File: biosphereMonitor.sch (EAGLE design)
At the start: 62 parts, among them IC1 XMEGA32A4AU, IC2 LM35, IC3 FT232RL, IC4 NE555D, IC5 SST25VF040, Q1 16Mhz, Q2 32kHz

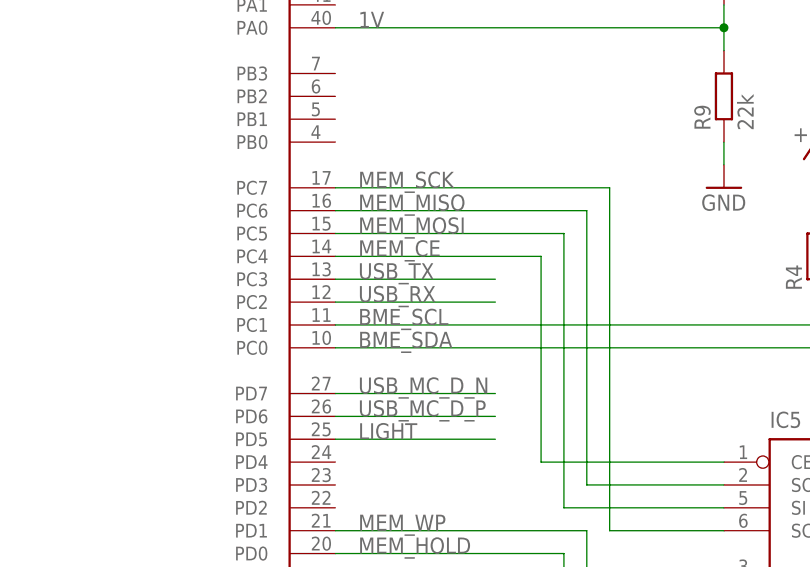
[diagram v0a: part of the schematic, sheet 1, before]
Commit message: changed rx with tx
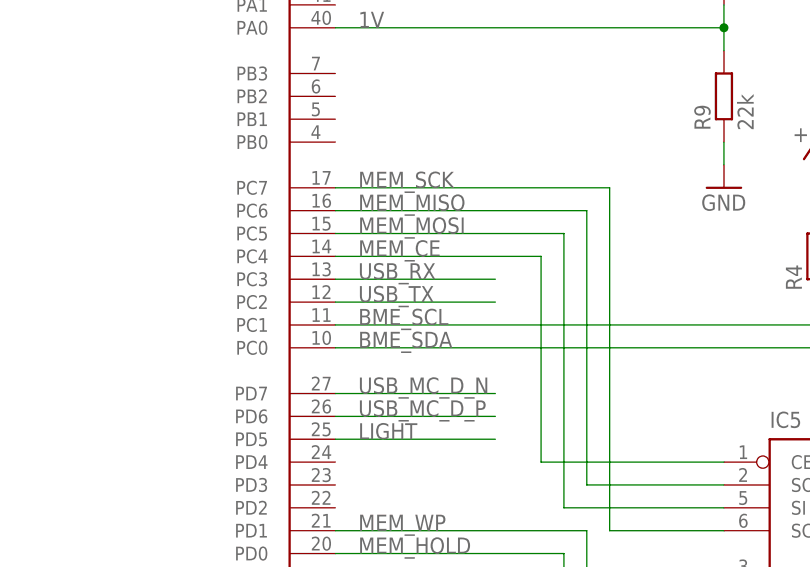
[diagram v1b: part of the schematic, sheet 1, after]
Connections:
- net USB_RX: now also IC1.PC3; no longer IC1.PC2
- net USB_TX: now also IC1.PC2; no longer IC1.PC3
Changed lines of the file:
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@@
 <net name="USB_RX" class="0">
-<segment>
-<pinref part="IC1" gate="G$1" pin="PC2"/>
-<wire x1="27.94" y1="-10.16" x2="45.72" y2="-10.16" width="0.1524" layer="91"/>
-<label x="30.48" y="-10.16" size="1.778" layer="95"/>
-</segment>
-</net>
-<net name="USB_TX" class="0">
 <segment>
 <pinref part="IC1" gate="G$1" pin="PC3"/>
@@
 </segment>
 </net>
+<net name="USB_TX" class="0">
+<segment>
+<pinref part="IC1" gate="G$1" pin="PC2"/>
+<wire x1="27.94" y1="-10.16" x2="45.72" y2="-10.16" width="0.1524" layer="91"/>
+<label x="30.48" y="-10.16" size="1.778" layer="95"/>
+</segment>
+</net>
